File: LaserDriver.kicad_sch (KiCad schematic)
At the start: 29 parts, among them J100 Screw_Terminal_01x04, J102 Screw_Terminal_01x02, U100 TPS92513DGQR

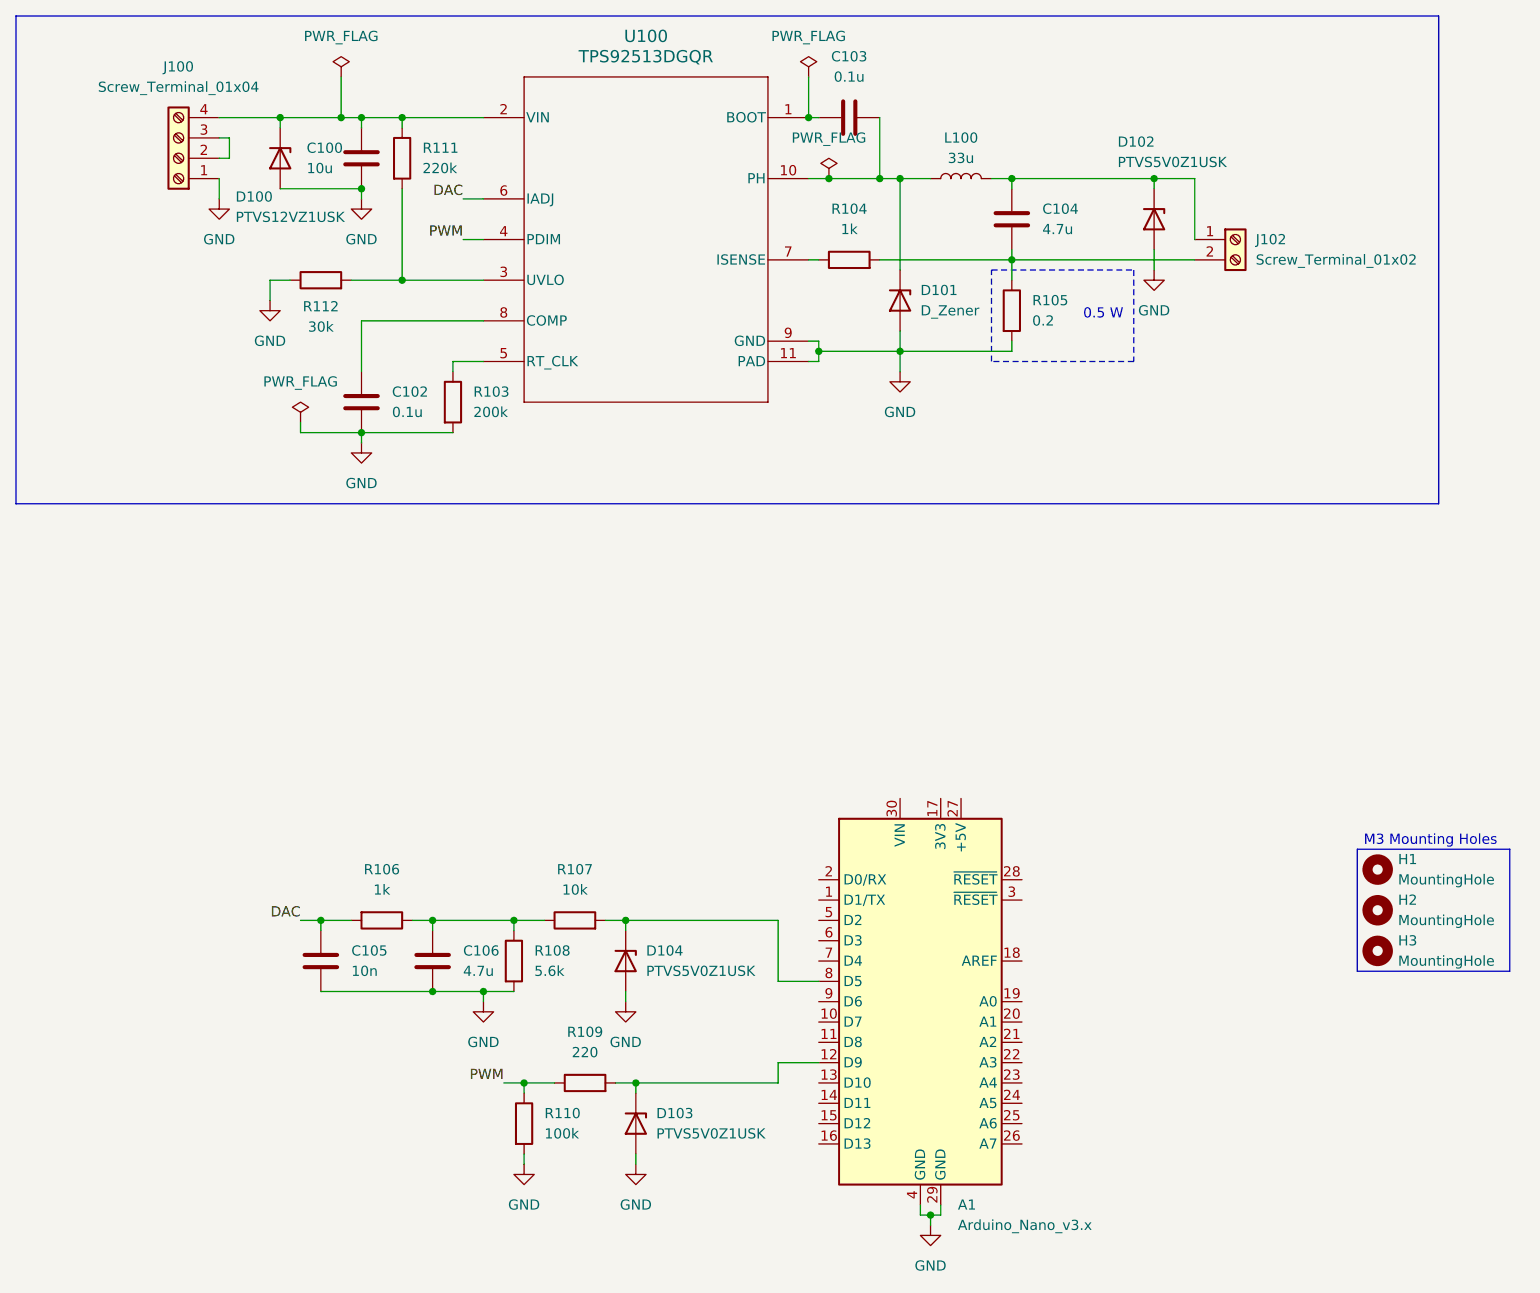
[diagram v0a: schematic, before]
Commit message: corrected arduino footprint
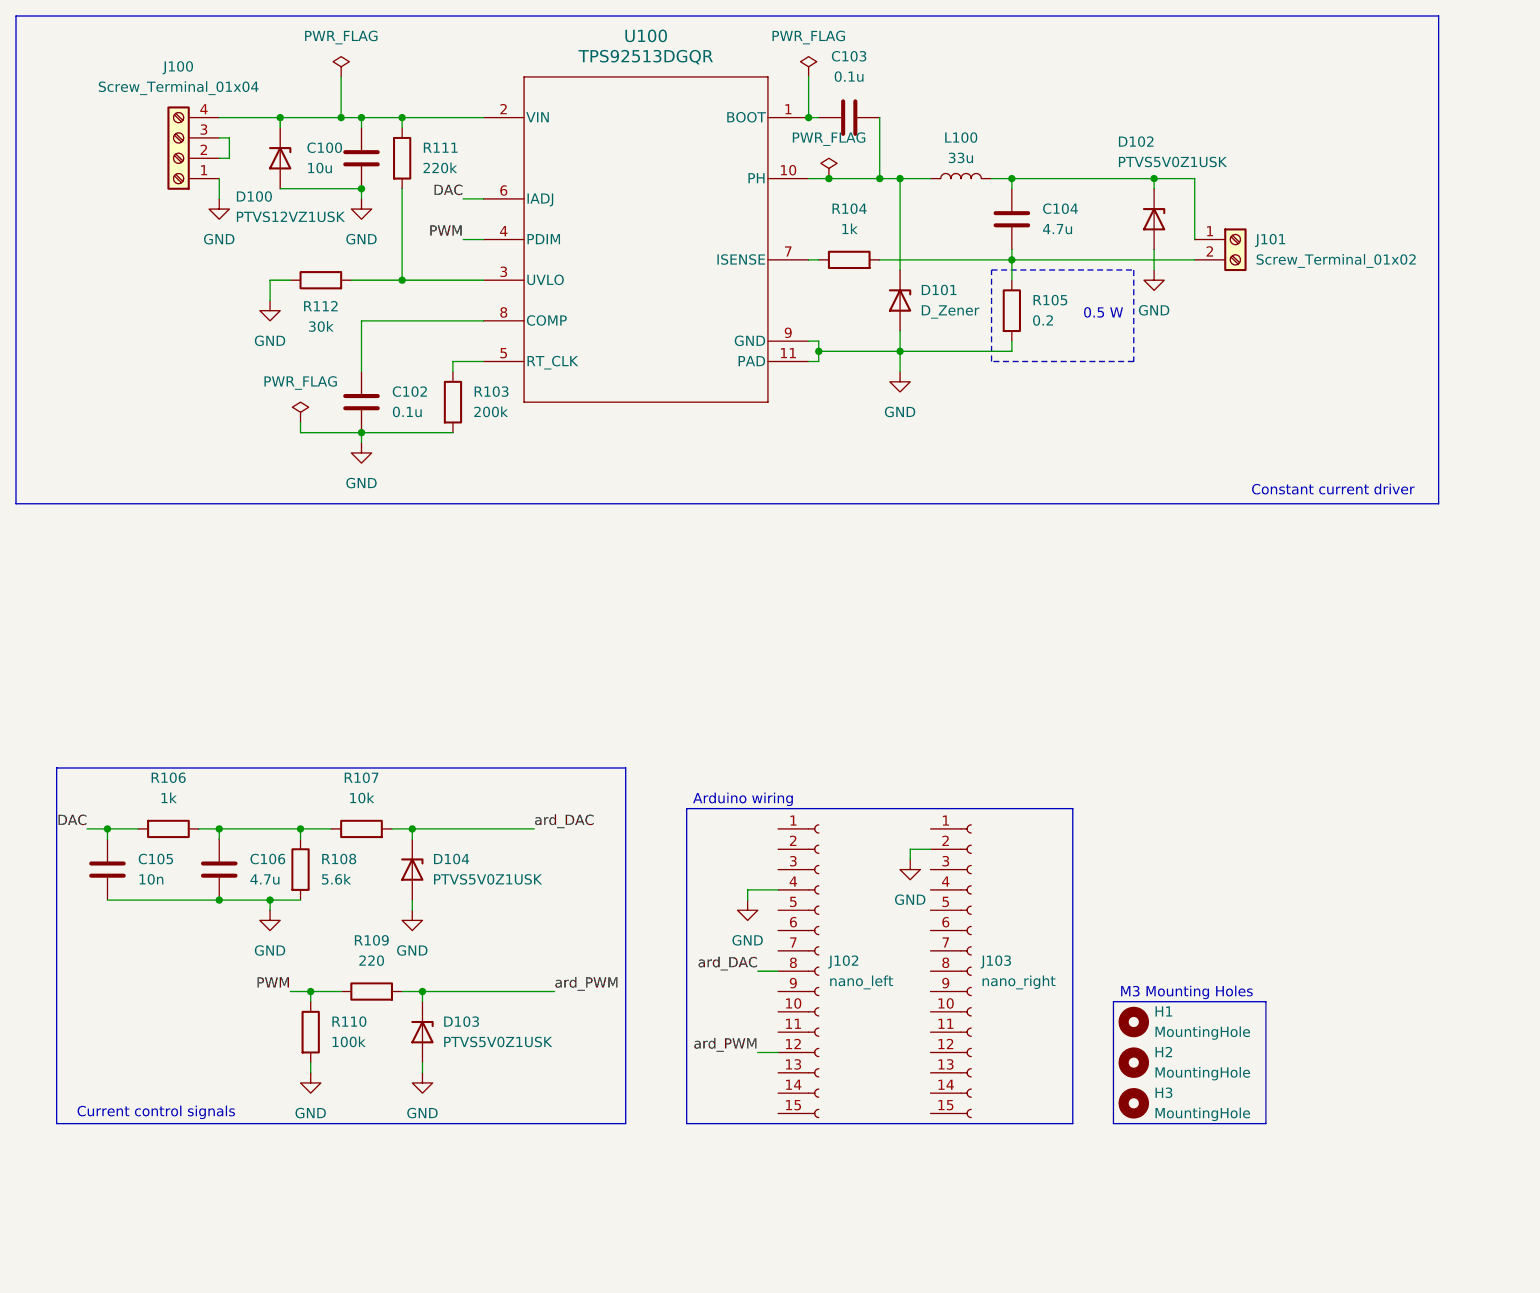
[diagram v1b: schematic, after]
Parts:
- removed A1: Arduino_Nano_v3.x, Arduino:Arduino_Nano, symbol MCU_Module:Arduino_Nano_v3.x
- added J102: nano_left, Connector_PinSocket_2.54mm:PinSocket_1x15_P2.54mm_Vertical, symbol Connector:Conn_01x15_Socket
- added J103: nano_right, Connector_PinSocket_2.54mm:PinSocket_1x15_P2.54mm_Vertical, symbol Connector:Conn_01x15_Socket
- renumbered J102 to J101
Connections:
- net GND: now also J102.4 (Pin_4), J103.2 (Pin_2)
- net ard_DAC: now reaches D104.1 (K), R107.2
- net ard_DAC: now also J102.8 (Pin_8)
- net ard_PWM: now reaches D103.1 (K), R109.2
- net ard_PWM: now also J102.12 (Pin_12)
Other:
- note added: "Arduino wiring"
- note added: "Constant current driver"
- note added: "Current control signals"
- moved on the sheet: C105, C106, D103, D104, H1, H2, H3, R106, R107, R108, R109, R110

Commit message: fixed errors
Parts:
- U100: footprint TPS:DGQ0010D_L -> TPS:DGQ0010D_NV_L
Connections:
- net at C104.1, D102.1 (K), L100.2: now also J101.2 (Pin_2); no longer J101.1 (Pin_1)
- net at C104.2, R104.2, R105.1: now also J101.1 (Pin_1); no longer J101.2 (Pin_2)
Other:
- moved on the sheet: J101
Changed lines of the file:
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@@
 	(wire
 		(pts
+			(xy 173.99 49.53) (xy 173.99 52.07)
+		)
+		(stroke
+			(width 0)
+			(type default)
+		)
+	)
+	(wire
+		(pts
 			(xy 33.02 120.65) (xy 36.83 120.65)
 		)
@@
 	(wire
 		(pts
-			(xy 163.83 39.37) (xy 168.91 39.37)
+			(xy 163.83 39.37) (xy 171.45 39.37)
 		)
 		(stroke
@@
 	(wire
 		(pts
-			(xy 168.91 39.37) (xy 168.91 46.99)
+			(xy 171.45 39.37) (xy 171.45 52.07)
 		)
 		(stroke
@@
 	(wire
 		(pts
-			(xy 146.05 49.53) (xy 168.91 49.53)
+			(xy 146.05 49.53) (xy 173.99 49.53)
 		)
 		(stroke
@@
 	(symbol
 		(lib_id "Connector:Screw_Terminal_01x02")
-		(at 173.99 46.99 0)
+		(at 173.99 57.15 270)
 		(unit 1)
 		(exclude_from_sim no)
@@
 		(on_board yes)
 		(dnp no)
-		(fields_autoplaced yes)
 		(property "Reference" "J101"
-			(at 176.53 46.9899 0)
+			(at 164.592 59.944 90)
 			(effects
 				(font
@@
 		)
 		(property "Value" "Screw_Terminal_01x02"
-			(at 176.53 49.5299 0)
+			(at 164.592 62.484 90)
 			(effects
 				(font
@@
 		)
 		(property "Footprint" "TerminalBlock:TerminalBlock_Xinya_XY308-2.54-2P_1x02_P2.54mm_Horizontal"
-			(at 173.99 46.99 0)
+			(at 173.99 57.15 0)
 			(effects
 				(font
@@
 		)
 		(property "Datasheet" "~"
-			(at 173.99 46.99 0)
+			(at 173.99 57.15 0)
 			(effects
 				(font
@@
 		)
 		(property "Description" "Generic screw terminal, single row, 01x02, script generated (kicad-library-utils/schlib/autogen/connector/)"
-			(at 173.99 46.99 0)
+			(at 173.99 57.15 0)
 			(effects
 				(font
@@
 		(on_board yes)
 		(dnp no)
-		(fields_autoplaced yes)
 		(property "Reference" "#FLG02"
 			(at 123.19 37.465 0)
@@
 		)
 		(property "Value" "PWR_FLAG"
-			(at 123.19 34.29 0)
+			(at 123.19 35.306 0)
 			(effects
 				(font
@@
 			)
 		)
-		(property "Footprint" "TPS:DGQ0010D_L"
+		(property "Footprint" "TPS:DGQ0010D_NV_L"
 			(at 100.33 46.99 0)
 			(effects

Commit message: added poors for ground
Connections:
- net intersection: now reaches C106.1, R106.1, R107.1, R108.1
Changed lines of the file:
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@@
+	)
+	(junction
+		(at 50.8 120.65)
+		(diameter 0)
+		(color 0 0 0 0)
 	)
 	(junction
@@
 	(wire
 		(pts
-			(xy 46.99 120.65) (xy 57.15 120.65)
+			(xy 46.99 120.65) (xy 50.8 120.65)
+		)
+		(stroke
+			(width 0)
+			(type default)
+		)
+	)
+	(wire
+		(pts
+			(xy 50.8 120.65) (xy 57.15 120.65)
 		)
 		(stroke
@@
 		(pts
 			(xy 46.99 31.75) (xy 54.61 31.75)
+		)
+		(stroke
+			(width 0)
+			(type default)
+		)
+	)
+	(wire
+		(pts
+			(xy 50.8 118.11) (xy 50.8 120.65)
 		)
 		(stroke
@@
 		)
 	)
+	(label "intersection"
+		(at 50.8 118.11 0)
+		(effects
+			(font
+				(size 1.27 1.27)
+			)
+			(justify left bottom)
+		)
+	)

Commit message: created calculator sheets
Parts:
- removed D101: D_Zener, Diode_SMD:D_SMB, symbol Device:D_Zener
- added D101: D_Schottky, Diode_SMD:D_SMB, symbol Device:D_Schottky
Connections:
- net GND: now also D101.2 (A)
- net at C103.2, L100.1, U100.10 (PH): now also D101.1 (K)
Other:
- note added: "1 W"
- note removed: "0.5 W"
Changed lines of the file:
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@@
 		)
 	)
-	(text "0.5 W"
+	(text "1 W"
 		(exclude_from_sim no)
 		(at 157.48 56.388 0)
@@
 	)
 	(symbol
+		(lib_id "Device:D_Schottky")
+		(at 132.08 54.61 270)
+		(unit 1)
+		(exclude_from_sim no)
+		(in_bom yes)
+		(on_board yes)
+		(dnp no)
+		(property "Reference" "D101"
+			(at 119.634 53.086 90)
+			(effects
+				(font
+					(size 1.27 1.27)
+				)
+				(justify left)
+			)
+		)
+		(property "Value" "D_Schottky"
+			(at 119.634 55.626 90)
+			(effects
+				(font
+					(size 1.27 1.27)
+				)
+				(justify left)
+			)
+		)
+		(property "Footprint" "Diode_SMD:D_SMB"
+			(at 132.08 54.61 0)
+			(effects
+				(font
+					(size 1.27 1.27)
+				)
+				(hide yes)
+			)
+		)
+		(property "Datasheet" "~"
+			(at 132.08 54.61 0)
+			(effects
+				(font
+					(size 1.27 1.27)
+				)
+				(hide yes)
+			)
+		)
+		(property "Description" "Schottky diode"
+			(at 132.08 54.61 0)
+			(effects
+				(font
+					(size 1.27 1.27)
+				)
+				(hide yes)
+			)
+		)
+		(pin "1"
+		)
+		(pin "2"
+		)
+		(instances
+			(project ""
+				(path "/e8909e30-da70-4cda-aa2c-d92cdd96f174"
+					(reference "D101")
+					(unit 1)
+				)
+			)
+		)
+	)
+	(symbol
 		(lib_id "power:GND")
 		(at 133.35 124.46 0)
@@
 					(unit 1)
 				)
-			)
-		)
-	)
-	(symbol
-		(lib_id "Device:D_Zener")
-		(at 132.08 54.61 270)
-		(unit 1)
-		(exclude_from_sim no)
-		(in_bom yes)
-		(on_board yes)
-		(dnp no)
-		(fields_autoplaced yes)
-		(property "Reference" "D101"
-			(at 134.62 53.3399 90)
-			(effects
-				(font
-					(size 1.27 1.27)
-				)
-				(justify left)
-			)
-		)
-		(property "Value" "D_Zener"
-			(at 134.62 55.8799 90)
-			(effects
-				(font
-					(size 1.27 1.27)
-				)
-				(justify left)
-			)
-		)
-		(property "Footprint" "Diode_SMD:D_SMB"
-			(at 132.08 54.61 0)
-			(effects
-				(font
-					(size 1.27 1.27)
-				)
-				(hide yes)
-			)
-		)
-		(property "Datasheet" "~"
-			(at 132.08 54.61 0)
-			(effects
-				(font
-					(size 1.27 1.27)
-				)
-				(hide yes)
-			)
-		)
-		(property "Description" "Zener diode"
-			(at 132.08 54.61 0)
-			(effects
-				(font
-					(size 1.27 1.27)
-				)
-				(hide yes)
-			)
-		)
-		(pin "2"
-		)
-		(pin "1"
-		)
-		(instances
-			(project ""
-				(path "/e8909e30-da70-4cda-aa2c-d92cdd96f174"
-					(reference "D101")
-					(unit 1)
-				)

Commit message: changes to tps ground via
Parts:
- C100: Manufacturer (none) -> Samsung Electro-Mechanics; Manufacturer Part Number (none) -> CL31A106KAHNNNE

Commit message: extended BOM
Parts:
- C102, C103: Manufacturer (none) -> Samsung Electro-Mechanics; Manufacturer Part Number (none) -> CL10B104KB8NNNC
- C104, C106: Manufacturer (none) -> Samsung Electro-Mechanics; Manufacturer Part Number (none) -> CL21A475KAQNNNE
- C105: Manufacturer (none) -> KEMET; Manufacturer Part Number (none) -> C0805C103K8RACAUTO
- D101: Manufacturer (none) -> FUXINSEMI; Manufacturer Part Number (none) -> FLSM115JE3
- J100: Manufacturer (none) -> DORABO; Manufacturer Part Number (none) -> DB125-2.54-4P-GN-S
- J101: Manufacturer (none) -> DORABO; Manufacturer Part Number (none) -> DB125-2.54-2P-GN-S
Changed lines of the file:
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@@
 			)
 		)
-		(property "Manufacturer" ""
+		(property "Manufacturer" "Samsung Electro-Mechanics"
 			(at 146.05 44.45 0)
 			(effects
@@
 			)
 		)
-		(property "Manufacturer Part Number" ""
+		(property "Manufacturer Part Number" "CL21A475KAQNNNE"
 			(at 146.05 44.45 0)
 			(effects
@@
 			)
 		)
-		(property "Manufacturer" ""
+		(property "Manufacturer" "FUXINSEMI"
 			(at 132.08 54.61 90)
 			(effects
@@
 			)
 		)
-		(property "Manufacturer Part Number" ""
+		(property "Manufacturer Part Number" "FLSM115JE3"
 			(at 132.08 54.61 90)
 			(effects
@@
 			)
 		)
-		(property "Manufacturer" ""
+		(property "Manufacturer" "DORABO"
 			(at 173.99 57.15 90)
 			(effects
@@
 			)
 		)
-		(property "Manufacturer Part Number" ""
+		(property "Manufacturer Part Number" "DB125-2.54-2P-GN-S"
 			(at 173.99 57.15 90)
 			(effects
@@
 			)
 		)
-		(property "Manufacturer" ""
+		(property "Manufacturer" "Samsung Electro-Mechanics"
 			(at 64.77 67.31 0)
 			(effects
@@
 			)
 		)
-		(property "Manufacturer Part Number" ""
+		(property "Manufacturer Part Number" "CL10B104KB8NNNC"
 			(at 64.77 67.31 0)
 			(effects
@@
 			)
 		)
-		(property "Manufacturer" ""
+		(property "Manufacturer" "KEMET"
 			(at 33.02 125.73 0)
 			(effects
@@
 			)
 		)
-		(property "Manufacturer Part Number" ""
+		(property "Manufacturer Part Number" "C0805C103K8RACAUTO"
 			(at 33.02 125.73 0)
 			(effects
@@
 			)
 		)
-		(property "Manufacturer" ""
+		(property "Manufacturer" "Samsung Electro-Mechanics"
 			(at 125.73 31.75 90)
 			(effects
@@
 			)
 		)
-		(property "Manufacturer Part Number" ""
+		(property "Manufacturer Part Number" "CL10B104KB8NNNC"
 			(at 125.73 31.75 90)
 			(effects
@@
 			)
 		)
-		(property "Manufacturer" ""
+		(property "Manufacturer" "DORABO"
 			(at 41.91 36.83 0)
 			(effects
@@
 			)
 		)
-		(property "Manufacturer Part Number" ""
+		(property "Manufacturer Part Number" "DB125-2.54-4P-GN-S"
 			(at 41.91 36.83 0)
 			(effects
@@
 			)
 		)
-		(property "Manufacturer" ""
+		(property "Manufacturer" "Samsung Electro-Mechanics"
 			(at 46.99 125.73 0)
 			(effects
@@
 			)
 		)
-		(property "Manufacturer Part Number" ""
+		(property "Manufacturer Part Number" "CL21A475KAQNNNE"
 			(at 46.99 125.73 0)
 			(effects

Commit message: finished BOM
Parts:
- removed D100: PTVS12VZ1USK, Diode_SMD:Nexperia_DSN1608-2_1.6x0.8mm, symbol Diode:PTVS12VZ1USK
- removed D102, D103, D104: PTVS5V0Z1USK, Diode_SMD:Nexperia_DSN1608-2_1.6x0.8mm, symbol Diode:PTVS5V0Z1USK
- added D100: PTVS20VZ1USK, Diode_SMD:Nexperia_DSN1608-2_1.6x0.8mm, symbol Diode:PTVS20VZ1USK
- added D102, D103, D104: PTVS10VZ1USK, Diode_SMD:Nexperia_DSN1608-2_1.6x0.8mm, symbol Diode:PTVS10VZ1USK
- J102, J103: Manufacturer (none) -> Megastar; Manufacturer Part Number (none) -> ZX-PM2.54-1-15PY
- L100: Manufacturer (none) -> PULSE; Manufacturer Part Number (none) -> PA4308.333NLT
- R103: Manufacturer (none) -> YAGEO; Manufacturer Part Number (none) -> RC0603FR-07200KL
- R104, R106: Manufacturer (none) -> YAGEO; Manufacturer Part Number (none) -> RC0603FR-071KL
- R105: Manufacturer (none) -> TA-I Tech; Manufacturer Part Number (none) -> RLP25FEER200
- R107: Manufacturer (none) -> YAGEO; Manufacturer Part Number (none) -> RC0603FR-0710KL
- R108: Manufacturer (none) -> YAGEO; Manufacturer Part Number (none) -> RC0603FR-075K6L
- R109: Manufacturer (none) -> YAGEO; Manufacturer Part Number (none) -> RC0603FR-07220RL
- R110: Manufacturer (none) -> YAGEO; Manufacturer Part Number (none) -> RC0603FR-07100KL
- R111: Manufacturer (none) -> YAGEO; Manufacturer Part Number (none) -> RC0603FR-07220KL
- R112: Manufacturer (none) -> YAGEO; Manufacturer Part Number (none) -> RC0603FR-0730KL
- U100: Manufacturer (none) -> Texas Instruments; Manufacturer Part Number (none) -> TPS92513DGQR
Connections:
- net GND: now also D100.2 (A), D102.2 (A), D103.2 (A), D104.2 (A)
- net ard_DAC: now also D103.1 (K)
- net ard_PWM: now also D104.1 (K)
- net at C104.1, J101.2 (Pin_2), L100.2: now also D102.1 (K)
- net at C100.1, J100.4 (Pin_4), R111.1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: now also D100.1 (K)
